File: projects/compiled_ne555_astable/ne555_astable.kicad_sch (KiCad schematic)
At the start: 7 parts, among them U1 NE555

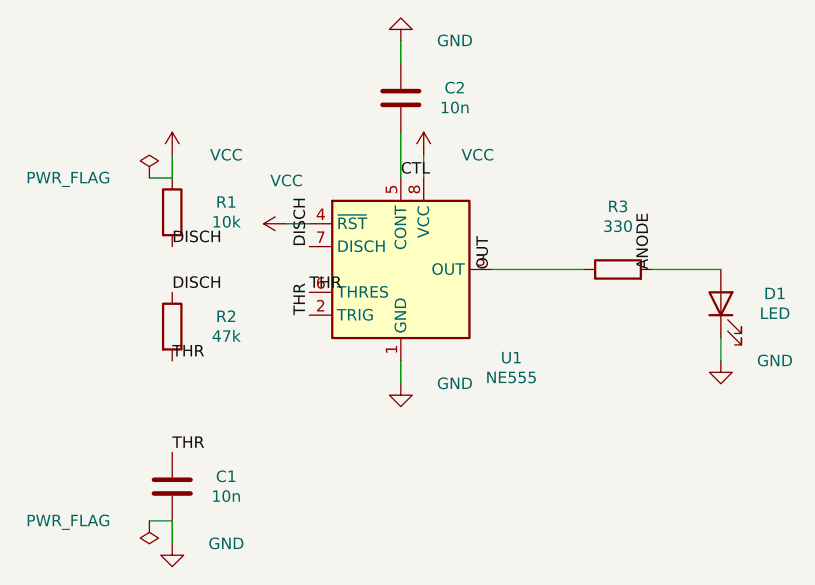
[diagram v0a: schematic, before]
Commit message: F5: human-quality pass — weld, route beauty, silent flags, design guide
The user's mandate: schematics must read as hand-drawn — tidy wires over
tag pairs, clean corners, nothing on screen but symbol, model and value.

- internal/place2/weld: same-net label islands get welded into real wires
  (straight/L/Z) whenever a clean corridor exists; every candidate is
  validated against gate.Check and reverted on any new violation. Redundant
  labels removed, one kept as documentation.
- routeNets beauty policy: a path with more than 3 bends or >70% detour
  over Manhattan distance reads worse than a label — demoted before it is
  ever drawn. Combined with weld this replaces snakes with short wires.
- PWR_FLAG value text hidden (sexp.HidePropertyText): the flag exists for
  ERC, not for the reader.
- design_guide: human-schematic conventions (signal flow, wire-vs-label,
  spacing recipes in grid cells, iteration protocol) distilled from
  SparkFun/KLC/IEEE-315/Altium/H&H research, embedded in the binary and
  served as an MCP tool for authoring LLMs.
- Crystal clusters reworked in both MCU sources: vertical crystal, straight
  XTAL1, single-L XTAL2, horizontal load caps — full Pierce oscillator
  wiring, zero label pairs. NE555 timing chain now fully wired via weld.

Co-Authored-By: Claude Fable 5 <noreply@anthropic.com>
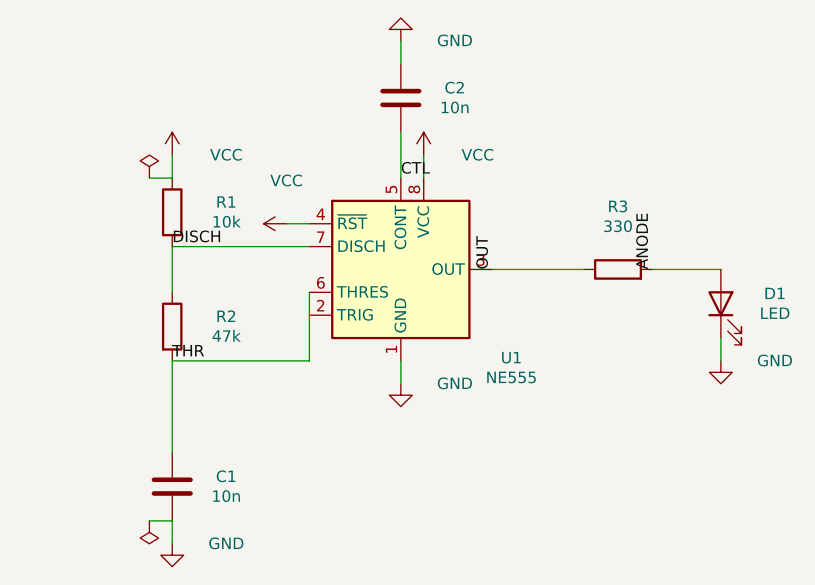
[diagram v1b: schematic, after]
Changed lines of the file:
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@@
     (instances
       (project ""
-        (path "/c0c5b0f8-6430-4d3f-9169-ee1da327ad5e" (reference "U1") (unit 1)))))
+        (path "/596bd98b-87a5-41ac-8f7d-913225de2c66" (reference "U1") (unit 1)))))
   (symbol (lib_id "Device:R")
     (at 27.94 41.91 0) (unit 1) (exclude_from_sim no) (in_bom yes) (on_board yes) (dnp no)
@@
     (instances
       (project ""
-        (path "/c0c5b0f8-6430-4d3f-9169-ee1da327ad5e" (reference "R1") (unit 1)))))
+        (path "/596bd98b-87a5-41ac-8f7d-913225de2c66" (reference "R1") (unit 1)))))
   (symbol (lib_id "Device:R")
     (at 27.94 54.61 0) (unit 1) (exclude_from_sim no) (in_bom yes) (on_board yes) (dnp no)
@@
     (instances
       (project ""
-        (path "/c0c5b0f8-6430-4d3f-9169-ee1da327ad5e" (reference "R2") (unit 1)))))
+        (path "/596bd98b-87a5-41ac-8f7d-913225de2c66" (reference "R2") (unit 1)))))
   (symbol (lib_id "Device:C")
     (at 27.94 72.39 0) (unit 1) (exclude_from_sim no) (in_bom yes) (on_board yes) (dnp no)
@@
     (instances
       (project ""
-        (path "/c0c5b0f8-6430-4d3f-9169-ee1da327ad5e" (reference "C1") (unit 1)))))
+        (path "/596bd98b-87a5-41ac-8f7d-913225de2c66" (reference "C1") (unit 1)))))
   (symbol (lib_id "Device:C")
     (at 53.34 29.21 180) (unit 1) (exclude_from_sim no) (in_bom yes) (on_board yes) (dnp no)
@@
     (instances
       (project ""
-        (path "/c0c5b0f8-6430-4d3f-9169-ee1da327ad5e" (reference "C2") (unit 1)))))
+        (path "/596bd98b-87a5-41ac-8f7d-913225de2c66" (reference "C2") (unit 1)))))
   (symbol (lib_id "Device:R")
     (at 77.47 48.26 90) (unit 1) (exclude_from_sim no) (in_bom yes) (on_board yes) (dnp no)
@@
     (instances
       (project ""
-        (path "/c0c5b0f8-6430-4d3f-9169-ee1da327ad5e" (reference "R3") (unit 1)))))
+        (path "/596bd98b-87a5-41ac-8f7d-913225de2c66" (reference "R3") (unit 1)))))
   (symbol (lib_id "Device:LED")
     (at 88.9 52.07 90) (unit 1) (exclude_from_sim no) (in_bom yes) (on_board yes) (dnp no)
@@
     (instances
       (project ""
-        (path "/c0c5b0f8-6430-4d3f-9169-ee1da327ad5e" (reference "D1") (unit 1)))))
+        (path "/596bd98b-87a5-41ac-8f7d-913225de2c66" (reference "D1") (unit 1)))))
   (wire
     (pts (xy 88.9 48.26) (xy 81.28 48.26))
@@
     (instances
       (project ""
-        (path "/c0c5b0f8-6430-4d3f-9169-ee1da327ad5e" (reference "#PWR01") (unit 1)))))
+        (path "/596bd98b-87a5-41ac-8f7d-913225de2c66" (reference "#PWR01") (unit 1)))))
   (wire
     (pts (xy 53.34 58.42) (xy 53.34 60.96))
@@
     (instances
       (project ""
-        (path "/c0c5b0f8-6430-4d3f-9169-ee1da327ad5e" (reference "#PWR02") (unit 1)))))
+        (path "/596bd98b-87a5-41ac-8f7d-913225de2c66" (reference "#PWR02") (unit 1)))))
   (wire
     (pts (xy 27.94 76.2) (xy 27.94 78.74))
@@
     (instances
       (project ""
-        (path "/c0c5b0f8-6430-4d3f-9169-ee1da327ad5e" (reference "#PWR03") (unit 1)))))
+        (path "/596bd98b-87a5-41ac-8f7d-913225de2c66" (reference "#PWR03") (unit 1)))))
   (wire
     (pts (xy 53.34 25.4) (xy 53.34 22.86))
@@
     (instances
       (project ""
-        (path "/c0c5b0f8-6430-4d3f-9169-ee1da327ad5e" (reference "#PWR04") (unit 1)))))
+        (path "/596bd98b-87a5-41ac-8f7d-913225de2c66" (reference "#PWR04") (unit 1)))))
   (wire
     (pts (xy 88.9 55.88) (xy 88.9 58.42))
@@
     (instances
       (project ""
-        (path "/c0c5b0f8-6430-4d3f-9169-ee1da327ad5e" (reference "#PWR05") (unit 1)))))
+        (path "/596bd98b-87a5-41ac-8f7d-913225de2c66" (reference "#PWR05") (unit 1)))))
   (wire
     (pts (xy 55.88 38.1) (xy 55.88 35.56))
@@
     (instances
       (project ""
-        (path "/c0c5b0f8-6430-4d3f-9169-ee1da327ad5e" (reference "#PWR06") (unit 1)))))
+        (path "/596bd98b-87a5-41ac-8f7d-913225de2c66" (reference "#PWR06") (unit 1)))))
   (wire
     (pts (xy 43.18 43.18) (xy 40.64 43.18))
@@
     (instances
       (project ""
-        (path "/c0c5b0f8-6430-4d3f-9169-ee1da327ad5e" (reference "#PWR07") (unit 1)))))
+        (path "/596bd98b-87a5-41ac-8f7d-913225de2c66" (reference "#PWR07") (unit 1)))))
   (wire
     (pts (xy 27.94 38.1) (xy 27.94 35.56))
     (stroke (width 0) (type default)))
   (label "THR"
-    (at 43.18 53.34 270) (fields_autoplaced yes)
+    (at 27.94 58.42 180) (fields_autoplaced yes)
     (effects
       (font (size 1.27 1.27)) (justify left bottom))
@@
       (effects
         (font (size 1.27 1.27)) (hide yes))))
-  (label "THR"
-    (at 43.18 50.8 180) (fields_autoplaced yes)
+  (label "DISCH"
+    (at 27.94 45.72 180) (fields_autoplaced yes)
     (effects
       (font (size 1.27 1.27)) (justify left bottom))
@@
       (effects
         (font (size 1.27 1.27)) (hide yes))))
-  (label "THR"
-    (at 27.94 58.42 0) (fields_autoplaced yes)
-    (effects
-      (font (size 1.27 1.27)) (justify left bottom))
-    (property "Intersheet References" ""
-      (at 0 0 0)
-      (effects
-        (font (size 1.27 1.27)) (hide yes))))
-  (label "THR"
-    (at 27.94 68.58 0) (fields_autoplaced yes)
-    (effects
-      (font (size 1.27 1.27)) (justify left bottom))
-    (property "Intersheet References" ""
-      (at 0 0 0)
-      (effects
-        (font (size 1.27 1.27)) (hide yes))))
-  (label "DISCH"
-    (at 43.18 45.72 270) (fields_autoplaced yes)
-    (effects
-      (font (size 1.27 1.27)) (justify left bottom))
-    (property "Intersheet References" ""
-      (at 0 0 0)
-      (effects
-        (font (size 1.27 1.27)) (hide yes))))
-  (label "DISCH"
-    (at 27.94 45.72 0) (fields_autoplaced yes)
-    (effects
-      (font (size 1.27 1.27)) (justify left bottom))
-    (property "Intersheet References" ""
-      (at 0 0 0)
-      (effects
-        (font (size 1.27 1.27)) (hide yes))))
-  (label "DISCH"
-    (at 27.94 50.8 0) (fields_autoplaced yes)
-    (effects
-      (font (size 1.27 1.27)) (justify left bottom))
-    (property "Intersheet References" ""
-      (at 0 0 0)
-      (effects
-        (font (size 1.27 1.27)) (hide yes))))
+  (wire
+    (pts (xy 27.94 45.72) (xy 27.94 50.8))
+    (stroke (width 0) (type default)))
+  (wire
+    (pts (xy 27.94 45.72) (xy 43.18 45.72))
+    (stroke (width 0) (type default)))
+  (wire
+    (pts (xy 43.18 50.8) (xy 43.18 53.34))
+    (stroke (width 0) (type default)))
+  (wire
+    (pts (xy 27.94 58.42) (xy 27.94 68.58))
+    (stroke (width 0) (type default)))
+  (wire
+    (pts (xy 27.94 58.42) (xy 43.18 58.42))
+    (stroke (width 0) (type default)))
+  (wire
+    (pts (xy 43.18 58.42) (xy 43.18 53.34))
+    (stroke (width 0) (type default)))
   (symbol (lib_id "power:PWR_FLAG")
     (at 25.4 76.2 180) (unit 1) (exclude_from_sim no) (in_bom no) (on_board no) (dnp no)
@@
         (font (size 1.27 1.27)) (hide yes)))
     (property "Value" "PWR_FLAG"
-      (at 16.39 76.2 0)
-      (effects
-        (font (size 1.27 1.27))))
+      (at 25.4 78.74 0)
+      (effects
+        (font (size 1.27 1.27)) (hide yes)))
     (property "Footprint" ""
       (at 25.4 76.2 0)
@@
     (instances
       (project ""
-        (path "/c0c5b0f8-6430-4d3f-9169-ee1da327ad5e" (reference "#FLG01") (unit 1)))))
+        (path "/596bd98b-87a5-41ac-8f7d-913225de2c66" (reference "#FLG01") (unit 1)))))
   (wire
     (pts (xy 27.94 76.2) (xy 25.4 76.2))
@@
         (font (size 1.27 1.27)) (hide yes)))
     (property "Value" "PWR_FLAG"
-      (at 16.39 38.1 0)
-      (effects
-        (font (size 1.27 1.27))))
+      (at 25.4 35.56 0)
+      (effects
+        (font (size 1.27 1.27)) (hide yes)))
     (property "Footprint" ""
       (at 25.4 38.1 0)
@@
     (instances
       (project ""
-        (path "/c0c5b0f8-6430-4d3f-9169-ee1da327ad5e" (reference "#FLG02") (unit 1)))))
+        (path "/596bd98b-87a5-41ac-8f7d-913225de2c66" (reference "#FLG02") (unit 1)))))
   (wire
     (pts (xy 27.94 38.1) (xy 25.4 38.1))

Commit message: Body model sees real symbol graphics; quiet nets drop junction tags
User-reported flaws from visual review, both fixed at the root:

- Wires over symbol artwork: the body model was pin-derived and blind to
  drawn graphics — an op-amp triangle's vertices stick out beyond the pin
  box, so "legal" wires crossed the drawing. internal/sexp/graphics.go now
  parses rectangle/polyline/circle/arc/bezier extents per unit with the
  exact pin transform; metrics.BodyBBox unions them with the legacy box,
  clamped off pin tips (Device:LED's emission arrows overhang the cathode
  pin and would have swallowed it). NE5532 feedback: 8 stroke crossings
  through the triangle before, 0 after (loops now label pairs). The model
  also exposed genuinely bad baked geometry in mcu_minimal_atmega328's
  crystal — repositioned with the template contract intact.

- "ANODE" tag on a resistor leg: net names with a "_" prefix are now
  quiet — connectivity only, their documentation label is stripped at the
  end of compilation when the wiring alone keeps the net whole. Junction
  nodes (R->LED) stay unlabeled like in any hand-drawn schematic.

- Battery hump: led_18650 anchors R1 in the pin's exit direction; the
  design guide gains the "respect the pin's exit direction" and "internal
  junctions carry no tag" recipes.

Co-Authored-By: Claude Fable 5 <noreply@anthropic.com>
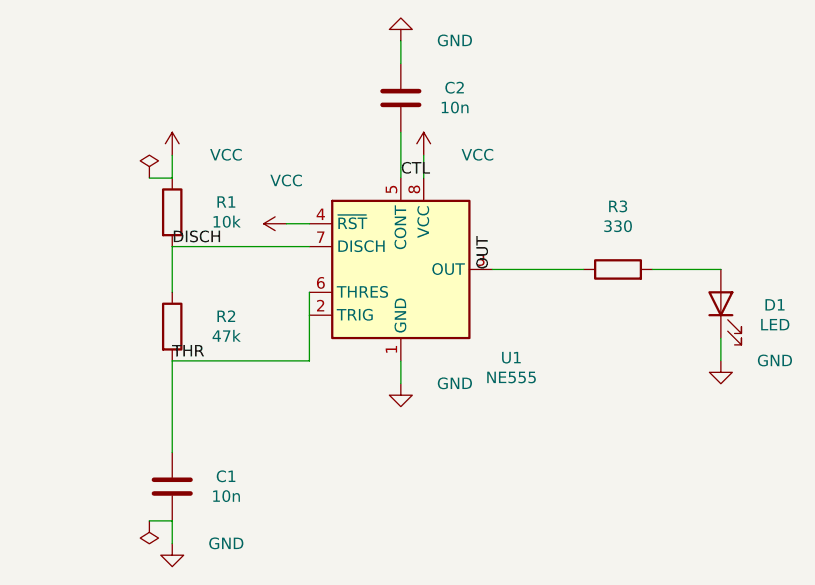
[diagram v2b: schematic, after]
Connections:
- net ANODE: no longer names the net of D1.2 (A), R3.2
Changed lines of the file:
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@@
     (instances
       (project ""
-        (path "/596bd98b-87a5-41ac-8f7d-913225de2c66" (reference "U1") (unit 1)))))
+        (path "/b9d5dce9-074d-468e-addc-3745baf03ca9" (reference "U1") (unit 1)))))
   (symbol (lib_id "Device:R")
     (at 27.94 41.91 0) (unit 1) (exclude_from_sim no) (in_bom yes) (on_board yes) (dnp no)
@@
     (instances
       (project ""
-        (path "/596bd98b-87a5-41ac-8f7d-913225de2c66" (reference "R1") (unit 1)))))
+        (path "/b9d5dce9-074d-468e-addc-3745baf03ca9" (reference "R1") (unit 1)))))
   (symbol (lib_id "Device:R")
     (at 27.94 54.61 0) (unit 1) (exclude_from_sim no) (in_bom yes) (on_board yes) (dnp no)
@@
     (instances
       (project ""
-        (path "/596bd98b-87a5-41ac-8f7d-913225de2c66" (reference "R2") (unit 1)))))
+        (path "/b9d5dce9-074d-468e-addc-3745baf03ca9" (reference "R2") (unit 1)))))
   (symbol (lib_id "Device:C")
     (at 27.94 72.39 0) (unit 1) (exclude_from_sim no) (in_bom yes) (on_board yes) (dnp no)
@@
     (instances
       (project ""
-        (path "/596bd98b-87a5-41ac-8f7d-913225de2c66" (reference "C1") (unit 1)))))
+        (path "/b9d5dce9-074d-468e-addc-3745baf03ca9" (reference "C1") (unit 1)))))
   (symbol (lib_id "Device:C")
     (at 53.34 29.21 180) (unit 1) (exclude_from_sim no) (in_bom yes) (on_board yes) (dnp no)
@@
     (instances
       (project ""
-        (path "/596bd98b-87a5-41ac-8f7d-913225de2c66" (reference "C2") (unit 1)))))
+        (path "/b9d5dce9-074d-468e-addc-3745baf03ca9" (reference "C2") (unit 1)))))
   (symbol (lib_id "Device:R")
     (at 77.47 48.26 90) (unit 1) (exclude_from_sim no) (in_bom yes) (on_board yes) (dnp no)
@@
     (instances
       (project ""
-        (path "/596bd98b-87a5-41ac-8f7d-913225de2c66" (reference "R3") (unit 1)))))
+        (path "/b9d5dce9-074d-468e-addc-3745baf03ca9" (reference "R3") (unit 1)))))
   (symbol (lib_id "Device:LED")
     (at 88.9 52.07 90) (unit 1) (exclude_from_sim no) (in_bom yes) (on_board yes) (dnp no)
     (property "Reference" "D1"
-      (at 94.91 50.97 90)
+      (at 94.91 52.24 90)
       (effects
         (font (size 1.27 1.27))))
     (property "Value" "LED"
-      (at 94.91 53.17 90)
+      (at 94.91 54.44 90)
       (effects
         (font (size 1.27 1.27))))
@@
     (instances
       (project ""
-        (path "/596bd98b-87a5-41ac-8f7d-913225de2c66" (reference "D1") (unit 1)))))
+        (path "/b9d5dce9-074d-468e-addc-3745baf03ca9" (reference "D1") (unit 1)))))
   (wire
     (pts (xy 88.9 48.26) (xy 81.28 48.26))
@@
     (pts (xy 53.34 38.1) (xy 53.34 33.02))
     (stroke (width 0) (type default)))
-  (label "ANODE"
-    (at 81.28 48.26 90) (fields_autoplaced yes)
-    (effects
-      (font (size 1.27 1.27)) (justify left bottom))
-    (property "Intersheet References" ""
-      (at 0 0 0)
-      (effects
-        (font (size 1.27 1.27)) (hide yes))))
   (label "CTL"
     (at 53.34 38.1 180) (fields_autoplaced yes)
@@
     (instances
       (project ""
-        (path "/596bd98b-87a5-41ac-8f7d-913225de2c66" (reference "#PWR01") (unit 1)))))
+        (path "/b9d5dce9-074d-468e-addc-3745baf03ca9" (reference "#PWR01") (unit 1)))))
   (wire
     (pts (xy 53.34 58.42) (xy 53.34 60.96))
@@
     (instances
       (project ""
-        (path "/596bd98b-87a5-41ac-8f7d-913225de2c66" (reference "#PWR02") (unit 1)))))
+        (path "/b9d5dce9-074d-468e-addc-3745baf03ca9" (reference "#PWR02") (unit 1)))))
   (wire
     (pts (xy 27.94 76.2) (xy 27.94 78.74))
@@
     (instances
       (project ""
-        (path "/596bd98b-87a5-41ac-8f7d-913225de2c66" (reference "#PWR03") (unit 1)))))
+        (path "/b9d5dce9-074d-468e-addc-3745baf03ca9" (reference "#PWR03") (unit 1)))))
   (wire
     (pts (xy 53.34 25.4) (xy 53.34 22.86))
@@
     (instances
       (project ""
-        (path "/596bd98b-87a5-41ac-8f7d-913225de2c66" (reference "#PWR04") (unit 1)))))
+        (path "/b9d5dce9-074d-468e-addc-3745baf03ca9" (reference "#PWR04") (unit 1)))))
   (wire
     (pts (xy 88.9 55.88) (xy 88.9 58.42))
@@
     (instances
       (project ""
-        (path "/596bd98b-87a5-41ac-8f7d-913225de2c66" (reference "#PWR05") (unit 1)))))
+        (path "/b9d5dce9-074d-468e-addc-3745baf03ca9" (reference "#PWR05") (unit 1)))))
   (wire
     (pts (xy 55.88 38.1) (xy 55.88 35.56))
@@
     (instances
       (project ""
-        (path "/596bd98b-87a5-41ac-8f7d-913225de2c66" (reference "#PWR06") (unit 1)))))
+        (path "/b9d5dce9-074d-468e-addc-3745baf03ca9" (reference "#PWR06") (unit 1)))))
   (wire
     (pts (xy 43.18 43.18) (xy 40.64 43.18))
@@
     (instances
       (project ""
-        (path "/596bd98b-87a5-41ac-8f7d-913225de2c66" (reference "#PWR07") (unit 1)))))
+        (path "/b9d5dce9-074d-468e-addc-3745baf03ca9" (reference "#PWR07") (unit 1)))))
   (wire
     (pts (xy 27.94 38.1) (xy 27.94 35.56))
@@
     (instances
       (project ""
-        (path "/596bd98b-87a5-41ac-8f7d-913225de2c66" (reference "#FLG01") (unit 1)))))
+        (path "/b9d5dce9-074d-468e-addc-3745baf03ca9" (reference "#FLG01") (unit 1)))))
   (wire
     (pts (xy 27.94 76.2) (xy 25.4 76.2))
@@
     (instances
       (project ""
-        (path "/596bd98b-87a5-41ac-8f7d-913225de2c66" (reference "#FLG02") (unit 1)))))
+        (path "/b9d5dce9-074d-468e-addc-3745baf03ca9" (reference "#FLG02") (unit 1)))))
   (wire
     (pts (xy 27.94 38.1) (xy 25.4 38.1))
